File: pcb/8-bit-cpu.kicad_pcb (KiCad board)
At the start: 2 copper layers, 122 x 81 mm, 16 parts, among them J1 Conn_01x24_Socket, J2 Conn_01x24_Socket, SW1 CLK MODE, SW2 CLK PULSE, SW3 BOOTLOAD EN, SW4 RAM MODE, SW5 RAM PULSE, U1 Tang Nano, U2 CA56-12EWA

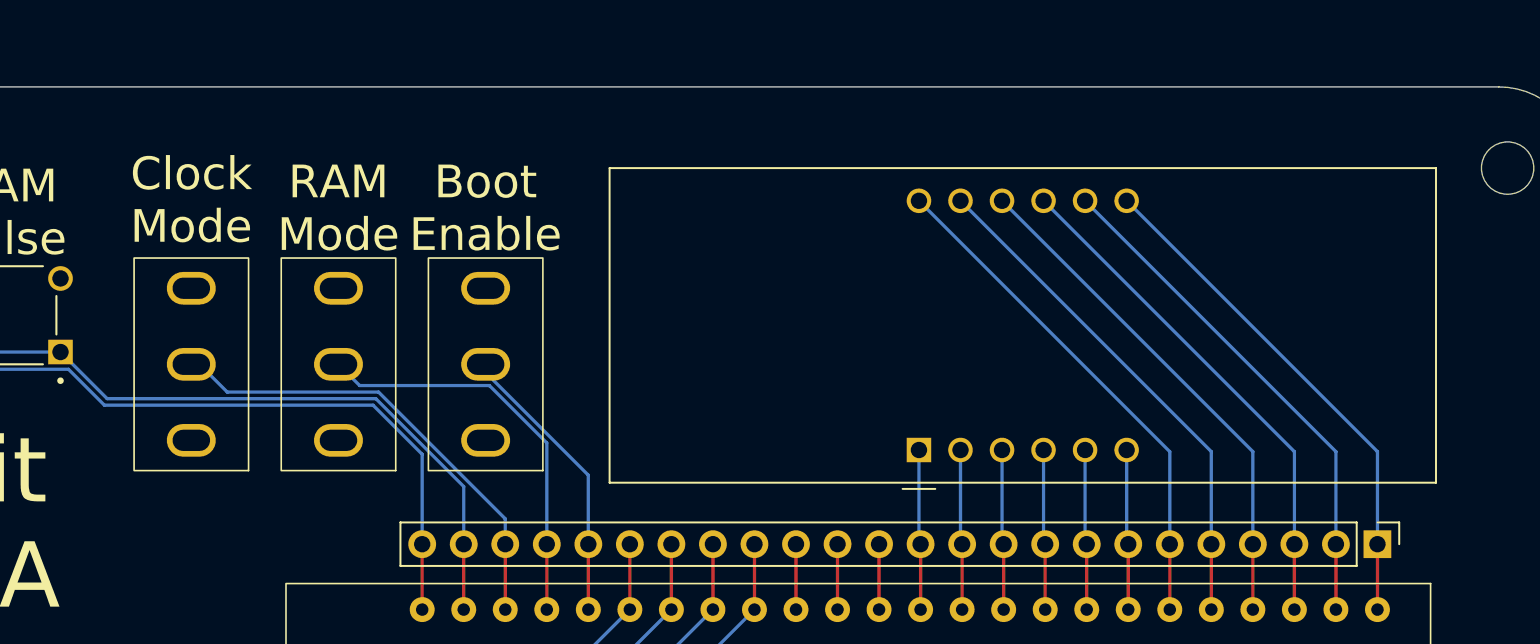
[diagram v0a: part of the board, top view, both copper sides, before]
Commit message: Added current limiting resistors to display
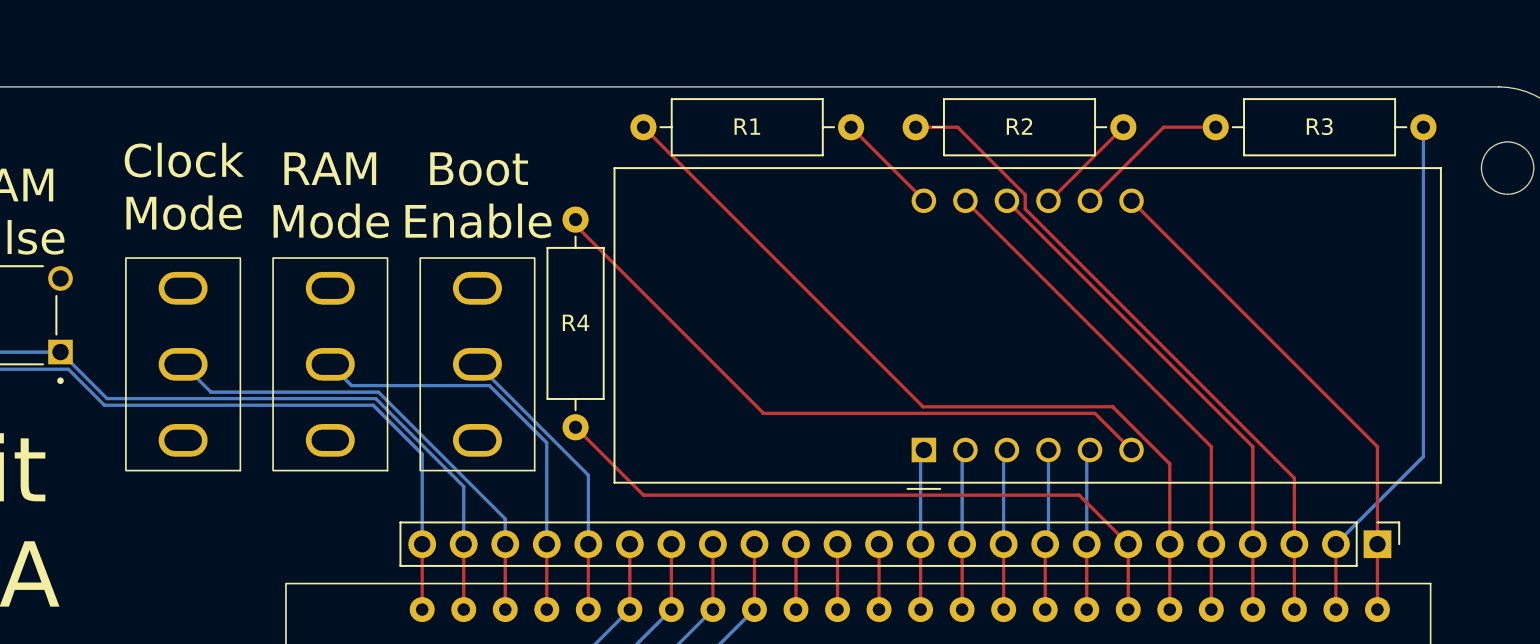
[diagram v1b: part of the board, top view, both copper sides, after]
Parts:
- added R1: 1k, Resistor_THT:R_Axial_DIN0309_L9.0mm_D3.2mm_P12.70mm_Horizontal, F.Cu at (132.8, 45.5)
- added R2: 1k, Resistor_THT:R_Axial_DIN0309_L9.0mm_D3.2mm_P12.70mm_Horizontal, F.Cu at (149.5, 45.5)
- added R3: 1k, Resistor_THT:R_Axial_DIN0309_L9.0mm_D3.2mm_P12.70mm_Horizontal, F.Cu at (155.2, 45.5)
- added R4: 1k, Resistor_THT:R_Axial_DIN0309_L9.0mm_D3.2mm_P12.70mm_Horizontal, F.Cu at (116.0, 51.1)
- moved SW1 0.50 mm to (92.0, 60.0)
- moved SW3 0.50 mm to (110.0, 60.0)
- moved SW4 0.50 mm to (101.0, 60.0)
- moved U2 0.30 mm to (137.3, 65.2)
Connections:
- U2 pad 12: /DIGIT 0 -> Net-(U2-CA1)
- U2 pad 6: /DIGIT 3 -> Net-(U2-CA4)
- U2 pad 8: /DIGIT 2 -> Net-(U2-CA3)
- U2 pad 9: /DIGIT 1 -> Net-(U2-CA2)
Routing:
- net Net-(U2-CA4): track 0.00 -> 40.0 mm
- net /DIGIT 3: track 9.80 -> 40.8 mm
- net /DIGIT 0: track 31.4 -> 49.6 mm
- net Net-(U2-CA3): track 0.00 -> 9.55 mm
- net /DIGIT 1: track 31.4 -> 40.6 mm
- net Net-(U2-CA2): track 0.00 -> 6.44 mm
- net Net-(U2-CA1): track 0.00 -> 6.34 mm
